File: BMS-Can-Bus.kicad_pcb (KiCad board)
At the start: 2 copper layers, 174 x 130.5 mm, 60 parts, among them J1 Conn_01x05, J2 Conn_01x02, Q1 dfsg1, Q2 dsg2, Q3 Q_PMOS_GSD, Q4 Q_PMOS_GSD, Q5 Q_PMOS_GSD, Q6 Q_PMOS_GSD, Q7 chg1, Q8 chg2, U1 BQ76952PFB, U2 STM32F103C8Tx, U4 SN65HVD230

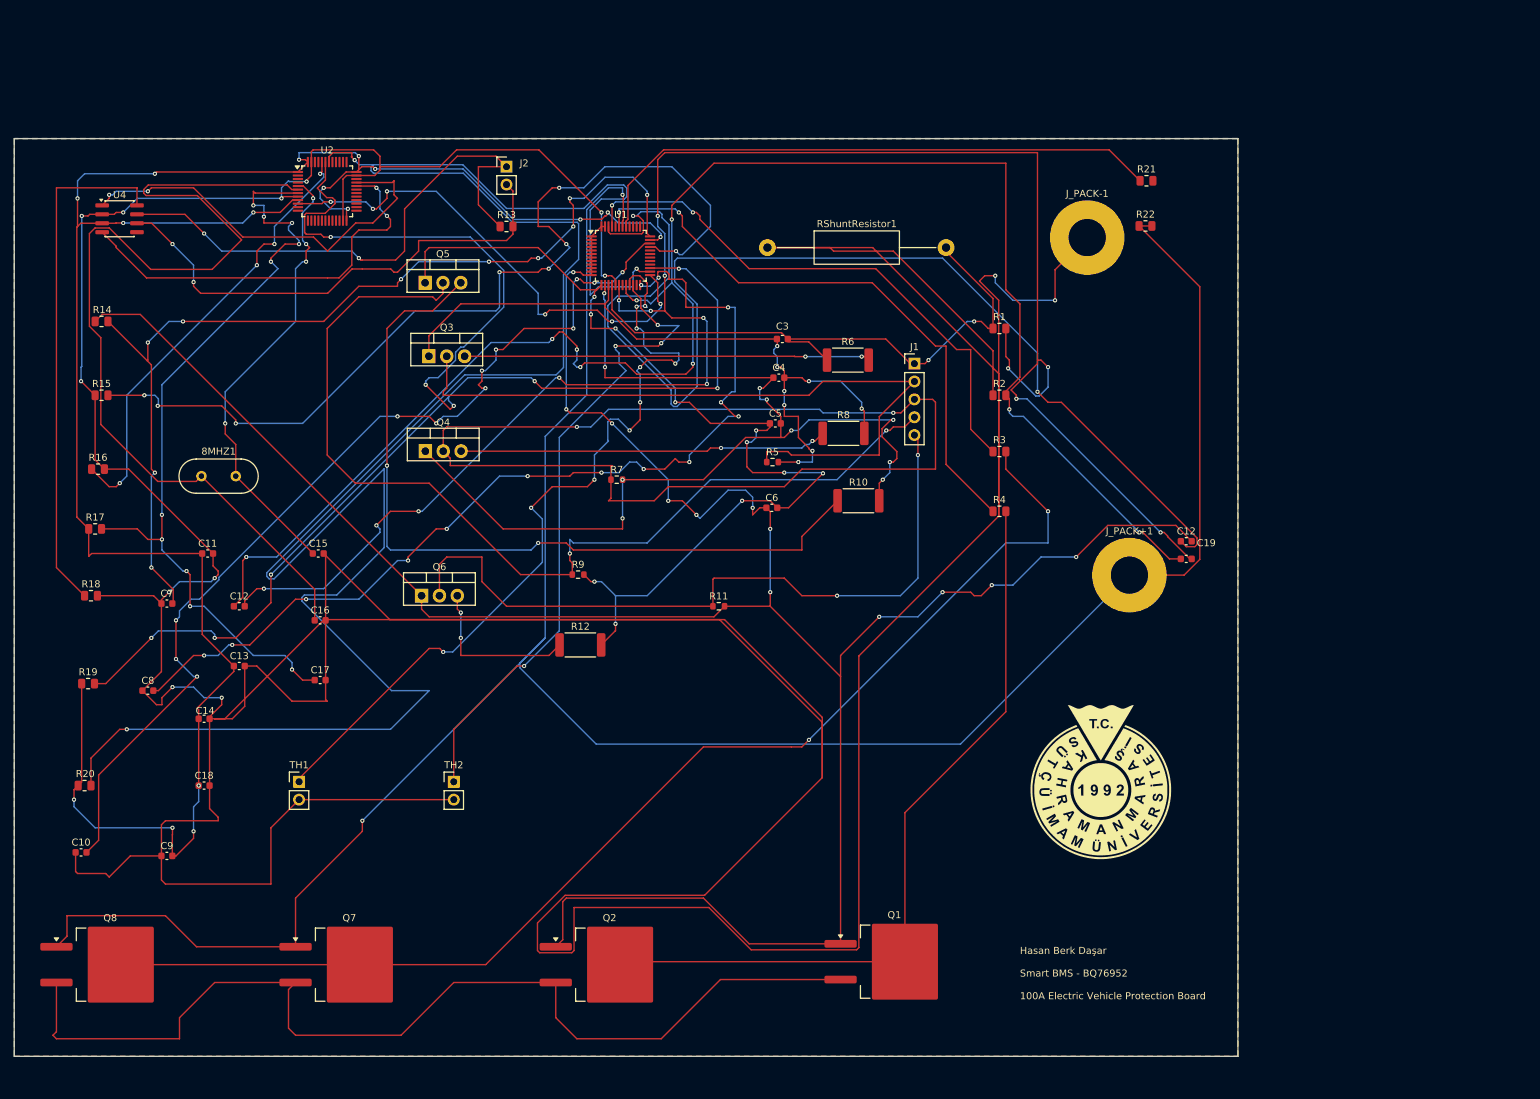
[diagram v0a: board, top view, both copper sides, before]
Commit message: Optimize PCB layout and power paths
High-current power paths refactored, decoupling capacitors optimized, and GND polygon pour added.
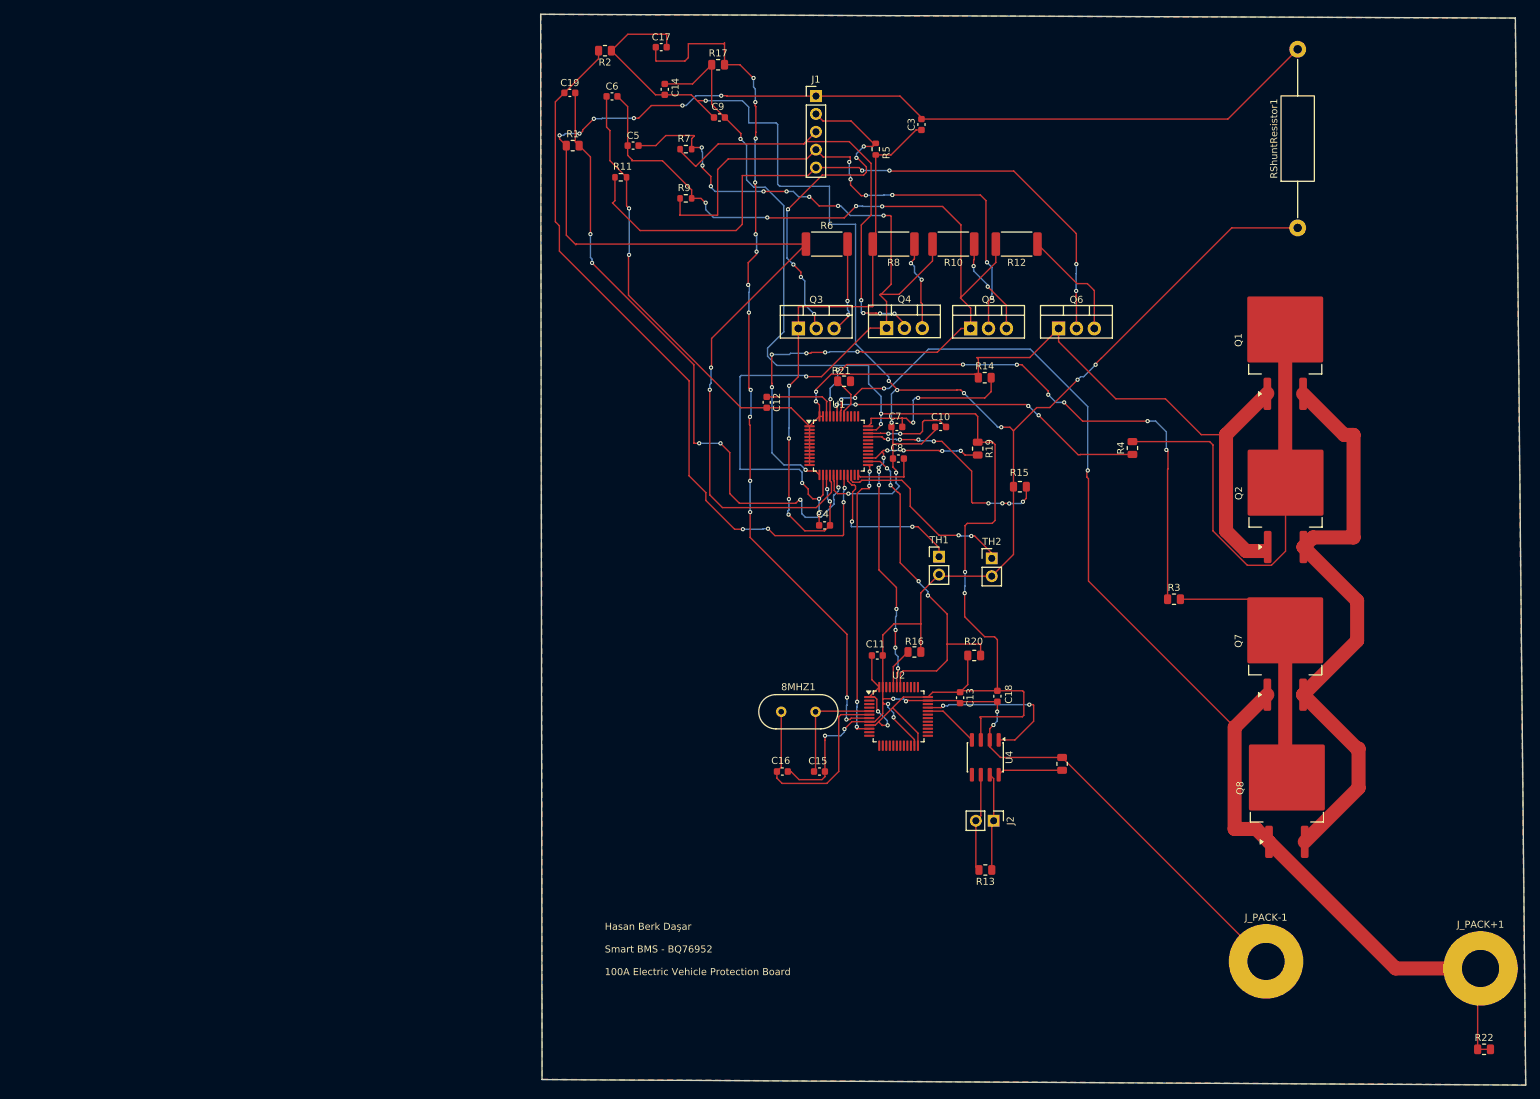
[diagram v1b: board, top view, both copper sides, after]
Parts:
- removed the C12 at (190.2, 87.3)
- removed the C12 at (55.5, 96.5)
- removed G***: LOGO, Library:ksulog2
- added C12: 100nF, Capacitor_SMD:C_0603_1608Metric, F.Cu at (130.5, 67.5)
- moved Q8 169.2 mm to (204.5, 122.3), turned to 90 degrees
- moved U4 145.0 mm to (161.6, 118.0), turned to -90 degrees
- moved Q7 140.8 mm to (204.2, 101.4), turned to 90 degrees
- moved R18 140.1 mm to (172.5, 118.9), turned to 90 degrees
- moved C10 136.4 mm to (155.2, 71.0)
- moved R15 131.2 mm to (166.5, 79.5)
- moved C9 131.1 mm to (123.8, 27.0)
- moved R19 130.8 mm to (160.5, 74.1), turned to -90 degrees
- moved R20 127.8 mm to (160.0, 103.5)
- moved R22 126.6 mm to (232.5, 159.5)
- moved R14 125.8 mm to (161.5, 64.0)
- moved R16 119.0 mm to (151.5, 103.0)
- moved Q2 117.2 mm to (204.3, 80.4), turned to 90 degrees
- moved J2 116.0 mm to (162.8, 127.0), turned to -90 degrees
- moved R13 114.1 mm to (161.6, 134.0), turned to 180 degrees
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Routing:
- net GND: track 908.1 -> 364.2 mm, vias 13 -> 18
- net /I2C_SCL: track 318.2 -> 49.9 mm, vias 3 -> 4
- net Net-(Q1-D): track 366.1 -> 176.2 mm, vias 12 -> 4
- net Net-(U1-SRP): track 273.2 -> 91.4 mm, vias 14 -> 6
- net Net-(J_PACK+1-Pin_1): track 343.9 -> 176.3 mm, vias 2 -> 4
- net Net-(U1-CP1): track 173.3 -> 11.0 mm, vias 2 -> 0
- net /I2C_SDA: track 209.7 -> 51.6 mm, vias 9 -> 12
- net Net-(J1-Pin_1): track 84.0 -> 225.1 mm, vias 2 -> 8
- net Net-(U1-SRN): track 244.2 -> 105.7 mm, vias 9 -> 4
- net Net-(Q7-G): track 172.2 -> 37.8 mm, vias 2 -> 0
- net Net-(U1-REG18): track 139.4 -> 9.24 mm, vias 14 -> 0
- net Net-(U1-REG2): track 140.7 -> 13.0 mm, vias 12 -> 2
- net Net-(U1-REGIN): track 138.5 -> 25.6 mm, vias 10 -> 2
- net Net-(U2-PD1): track 138.8 -> 31.8 mm
- net Net-(U1-RST_SHUT): track 133.4 -> 31.0 mm
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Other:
- board size 174 x 130.5 mm -> 140.1 x 152.3 mm

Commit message: docs: update specification to 5A continuous rating and finalize layout
update specification to 5A continuous rating and finalize layout
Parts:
- moved R22 1.60 mm to (232.7, 161.1)
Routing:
- net Net-(U1-CHG): track 82.4 -> 88.3 mm
- net GND: track 364.2 -> 368.7 mm
- net Net-(Q1-G): track 68.7 -> 72.7 mm
- net Net-(U1-DSG): track 46.7 -> 49.6 mm
- net Net-(J_PACK+1-Pin_1): track 176.3 -> 178.6 mm
- net Net-(J1-Pin_1): track 225.1 -> 226.3 mm
- net Net-(Q1-D): track 176.2 -> 175.4 mm
- net Net-(U1-LD): track 6.18 -> 5.45 mm
- net Net-(U1-REGIN): track 25.6 -> 24.9 mm
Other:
- board text added: "Hasan Berk Daşar Smart BMS - BQ76952 4S 15A"
- board text removed: "Hasan Berk Daşar Smart BMS - BQ76952 100A Electric Vehicle Protection Board"

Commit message: ERC warnning
Known open items: 2 ERC warnings remain unresolved (a GND net junction and the LD pin pull-up connection near R21) — likely a wire/grid-snap issue in the schematic editor that I couldn't fully trace. Flagging as a known limitation for this learning-stage design.
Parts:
- added J3: bat+, MountingHole:MountingHole_3.2mm_M3_Pad, F.Cu at (222.9, 57.1)
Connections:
- C12 pad 2: Net-(Q1-D) -> Net-(J3-Pin_1)
- C6 pad 1: Net-(Q1-D) -> Net-(J3-Pin_1)
- Q1 pad 2: Net-(Q1-G) -> Net-(J3-Pin_1)
- Q2 pad 2: Net-(Q1-G) -> Net-(J3-Pin_1)
- Q6 pad 1: Net-(Q1-D) -> Net-(J3-Pin_1)
- Q7 pad 1: Net-(J_PACK+1-Pin_1) -> Net-(Q7-D)
- Q7 pad 2: Net-(Q7-G) -> Net-(J_PACK+1-Pin_1)
- Q8 pad 1: Net-(J_PACK+1-Pin_1) -> Net-(Q7-D)
- Q8 pad 2: Net-(Q7-G) -> Net-(J_PACK+1-Pin_1)
- R11 pad 2: Net-(Q1-D) -> Net-(J3-Pin_1)
- R14 pad 1: Net-(Q1-D) -> Net-(J3-Pin_1)
- R21 pad 2: unconnected-(R21-Pad2) -> Net-(J_PACK+1-Pin_1)
- R3 pad 2: Net-(Q7-G) -> Net-(Q7-D)
- R4 pad 2: Net-(Q1-G) -> Net-(Q1-D)
- U1 pad 1: Net-(Q1-D) -> Net-(J3-Pin_1)
- U1 pad 10: Net-(Q1-D) -> Net-(J3-Pin_1)
- U1 pad 11: Net-(Q1-D) -> Net-(J3-Pin_1)
- U1 pad 12: Net-(Q1-D) -> Net-(J3-Pin_1)
- U1 pad 2: Net-(Q1-D) -> Net-(J3-Pin_1)
- U1 pad 3: Net-(Q1-D) -> Net-(J3-Pin_1)
- U1 pad 4: Net-(Q1-D) -> Net-(J3-Pin_1)
- U1 pad 47: Net-(Q1-D) -> Net-(J3-Pin_1)
- U1 pad 48: Net-(Q1-D) -> Net-(J3-Pin_1)
- U1 pad 5: Net-(Q1-D) -> Net-(J3-Pin_1)
- U1 pad 6: Net-(Q1-D) -> Net-(J3-Pin_1)
- U1 pad 7: Net-(Q1-D) -> Net-(J3-Pin_1)
- U1 pad 8: Net-(Q1-D) -> Net-(J3-Pin_1)
- U1 pad 9: Net-(Q1-D) -> Net-(J3-Pin_1)
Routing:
- net Net-(J3-Pin_1): track 0.00 -> 191.5 mm, vias 0 -> 8
- net Net-(Q1-D): track 175.4 -> 43.7 mm, vias 4 -> 0
- net Net-(Q1-G): track 72.7 -> 0.00 mm
- net Net-(Q7-D): track 0.00 -> 47.0 mm, vias 0 -> 2
- net Net-(Q7-G): track 37.7 -> 0.00 mm
- net Net-(J_PACK+1-Pin_1): track 178.6 -> 195.8 mm
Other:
- board text added: "Hasan Berk Daşar Smart BMS - BQ76952 4S 5A"
- board text removed: "Hasan Berk Daşar Smart BMS - BQ76952 4S 15A"

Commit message: Add files via upload
redesign PCB size
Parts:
- moved R22 30.4 mm to (210.3, 140.5)
- moved J_PACK-1 29.9 mm to (186.4, 121.3)
- moved J_PACK+1 18.8 mm to (219.5, 133.9)
- moved J3 6.42 mm to (216.5, 57.1)
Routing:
- net Net-(J_PACK+1-Pin_1): track 195.8 -> 167.8 mm
- net GND: track 368.7 -> 341.0 mm
- net Net-(J3-Pin_1): track 191.5 -> 186.5 mm
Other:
- board size 140.1 x 152.3 mm -> 127.7 x 130.5 mm
- board text removed: "Hasan Berk Daşar Smart BMS - BQ76952 4S 5A"
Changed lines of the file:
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@@
 	(footprint "MountingHole:MountingHole_5.3mm_M5_Pad"
 		(layer "F.Cu")
-		(at 201.5 147)
+		(at 186.3852 121.2596)
 		(descr "Mounting Hole 5.3mm, M5, generated by kicad-footprint-generator mountinghole.py")
 		(tags "mountinghole M5")
@@
 	(footprint "MountingHole:MountingHole_5.3mm_M5_Pad"
 		(layer "F.Cu")
-		(at 232 148)
+		(at 219.5322 133.9342)
 		(descr "Mounting Hole 5.3mm, M5, generated by kicad-footprint-generator mountinghole.py")
 		(tags "mountinghole M5")
@@
 	(footprint "Resistor_SMD:R_0805_2012Metric"
 		(layer "F.Cu")
-		(at 232.6894 161.0868)
+		(at 210.3374 140.5382)
 		(descr "Resistor SMD 0805 (2012 Metric), square (rectangular) end terminal, IPC-7351 nominal, (Body size source: IPC-SM-782 page 72, https://www.pcb-3d.com/wordpress/wp-content/uploads/ipc-sm-782a_amendment_1_and_2.pdf)")
 		(tags "resistor")
@@
 	(footprint "MountingHole:MountingHole_3.2mm_M3_Pad"
 		(layer "F.Cu")
-		(at 222.931 57.1198)
+		(at 216.5096 57.1246)
 		(descr "Mounting Hole 3.2mm, M3, generated by kicad-footprint-generator mountinghole.py")
 		(tags "mountinghole M3")
@@
 	(gr_line
 		(start 98.3488 12.319)
-		(end 98.552 163.8046)
+		(end 99.3013 142.3543)
 		(stroke
 			(width 0.05)
@@
 	)
 	(gr_line
-		(start 98.552 163.8046)
-		(end 238.4298 164.592)
+		(start 99.3013 142.3543)
+		(end 226.0092 142.8242)
 		(stroke
 			(width 0.05)
@@
 	)
 	(gr_line
-		(start 236.956202 12.862268)
+		(start 224.663 12.954)
 		(end 98.3488 12.319)
 		(stroke
@@
 	)
 	(gr_line
-		(start 238.4298 164.592)
-		(end 236.956202 12.862268)
+		(start 226.0092 142.8242)
+		(end 224.663 12.954)
 		(stroke
 			(width 0.05)
@@
 		(layer "Edge.Cuts")
 	)
-	(gr_text "Hasan Berk Daşar\n\nSmart BMS - BQ76952\n\n4S 5A"
-		(at 107.4674 149.0726 0)
-		(layer "F.SilkS")
-		(effects
-			(font
-				(size 1 1)
-				(thickness 0.1)
-			)
-			(justify left bottom)
-		)
-	)
 	(segment
 		(start 148.59 99.0092)
@@
 	)
 	(segment
+		(start 183.1256 118)
+		(end 186.3852 121.2596)
+		(width 2)
+		(layer "F.Cu")
+		(net "GND")
+	)
+	(segment
 		(start 148.45 75.5)
 		(end 148.45 73.3552)
@@
 	)
 	(segment
-		(start 172.5 118)
-		(end 175.7596 118)
-		(width 2)
-		(layer "F.Cu")
-		(net "GND")
-	)
-	(segment
 		(start 178.054 61.2648)
 		(end 178.0286 61.2648)
@@
 	)
 	(segment
-		(start 201.5 143.7404)
-		(end 201.5 147)
-		(width 2)
-		(layer "F.Cu")
-		(net "GND")
-	)
-	(segment
 		(start 153.4125 109.9125)
 		(end 150.7049 109.9125)
@@
 	)
 	(segment
-		(start 175.7596 118)
-		(end 201.5 143.7404)
-		(width 2)
-		(layer "F.Cu")
-		(net "GND")
-	)
-	(segment
 		(start 138.775 115.5806)
 		(end 138.7856 115.57)
@@
 	)
 	(segment
+		(start 172.5 118)
+		(end 183.1256 118)
+		(width 2)
+		(layer "F.Cu")
+		(net "GND")
+	)
+	(segment
 		(start 163.2966 111.4552)
 		(end 163.2712 111.4806)
@@
 	)
 	(segment
+		(start 204.2444 57.1246)
+		(end 204.225 57.144)
+		(width 0.2)
+		(layer "F.Cu")
+		(net "Net-(J3-Pin_1)")
+	)
+	(segment
 		(start 136.5875 71.4125)
 		(end 136.5875 71.9125)
@@
 	)
 	(segment
-		(start 222.931 57.1198)
-		(end 205.5492 57.1198)
-		(width 0.2)
-		(layer "F.Cu")
-		(net "Net-(J3-Pin_1)")
-	)
-	(segment
 		(start 139.6746 63.5)
 		(end 137.5156 65.659)
@@
 	)
 	(segment
+		(start 216.5096 57.1246)
+		(end 204.2444 57.1246)
+		(width 0.2)
+		(layer "F.Cu")
+		(net "Net-(J3-Pin_1)")
+	)
+	(segment
 		(start 136.5875 73.9125)
 		(end 136.5875 74.4125)
@@
 	)
 	(segment
-		(start 231.5875 148.4125)
-		(end 232 148)
+		(start 204.46 136.1848)
+		(end 208.8134 140.5382)
 		(width 0.2)
 		(layer "F.Cu")
@@
 	)
 	(segment
-		(start 216.2752 148)
-		(end 219.92 148)
+		(start 204.46 120.85)
+		(end 204.46 136.1848)
 		(width 0.2)
 		(layer "F.Cu")
@@
 	)
 	(segment
-		(start 231.7769 161.0868)
-		(end 233.6019 161.0868)
-		(width 2)
-		(layer "F.Cu")
-		(net "Net-(J_PACK+1-Pin_1)")
-	)
-	(segment
 		(start 204.225 120.615)
 		(end 204.46 120.85)
@@
 	)
 	(segment
-		(start 231.7769 159.6894)
-		(end 231.7769 161.0868)
-		(width 2)
-		(layer "F.Cu")
-		(net "Net-(J_PACK+1-Pin_1)")
-	)
-	(segment
 		(start 176.2506 92.9132)
 		(end 176.2506 78.359)
@@
 	)
 	(segment
-		(start 219.92 148)
-		(end 232 148)
-		(width 2)
-		(layer "F.Cu")
-		(net "Net-(J_PACK+1-Pin_1)")
-	)
-	(segment
 		(start 204.225 99.925)
 		(end 204.225 120.615)
@@
 	)
 	(segment
-		(start 204.46 120.85)
-		(end 204.46 136.1848)
-		(width 0.2)
-		(layer "F.Cu")
-		(net "Net-(J_PACK+1-Pin_1)")
-	)
-	(segment
-		(start 204.46 136.1848)
-		(end 216.2752 148)
-		(width 0.2)
-		(layer "F.Cu")
-		(net "Net-(J_PACK+1-Pin_1)")
-	)
-	(segment
 		(start 142.7125 64.8)
 		(end 142.4125 64.8)
@@
 	)
 	(segment
+		(start 209.4249 140.5382)
+		(end 211.2499 140.5382)
+		(width 0.2)
+		(layer "F.Cu")
+		(net "Net-(J_PACK+1-Pin_1)")
+	)
+	(segment
+		(start 211.2499 140.5382)
+		(end 212.9282 140.5382)
+		(width 0.2)
+		(layer "F.Cu")
+		(net "Net-(J_PACK+1-Pin_1)")
+	)
+	(segment
+		(start 208.8134 140.5382)
+		(end 209.4249 140.5382)
+		(width 0.2)
+		(layer "F.Cu")
+		(net "Net-(J_PACK+1-Pin_1)")
+	)
+	(segment
+		(start 212.9282 140.5382)
+		(end 219.5322 133.9342)
+		(width 0.2)
+		(layer "F.Cu")
+		(net "Net-(J_PACK+1-Pin_1)")
+	)
+	(segment
 		(start 140.4112 66.7258)
 		(end 141.097 67.4116)
@@
 	)
 	(segment
-		(start 231.5875 159.5)
-		(end 231.5875 148.4125)
-		(width 2)
-		(layer "F.Cu")
-		(net "Net-(J_PACK+1-Pin_1)")
-	)
-	(segment
 		(start 197.0278 113.6904)
 		(end 176.2506 92.9132)
@@
 	)
 	(segment
-		(start 231.5875 159.5)
-		(end 231.7769 159.6894)
-		(width 0.2)
-		(layer "F.Cu")
-		(net "Net-(J_PACK+1-Pin_1)")
-	)
-	(segment
 		(start 141 68.73009)
 		(end 141 69.5)
@@
 		(polygon
 			(pts
-				(xy 236.9312 12.8778) (xy 98.3742 12.3444) (xy 98.5774 163.7792) (xy 238.4044 164.5666)
+				(xy 224.6376 13.0556) (xy 98.3742 12.3444) (xy 98.9584 143.0274) (xy 226.2124 142.4686)
 			)
 		)
